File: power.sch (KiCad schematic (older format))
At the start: 3 parts

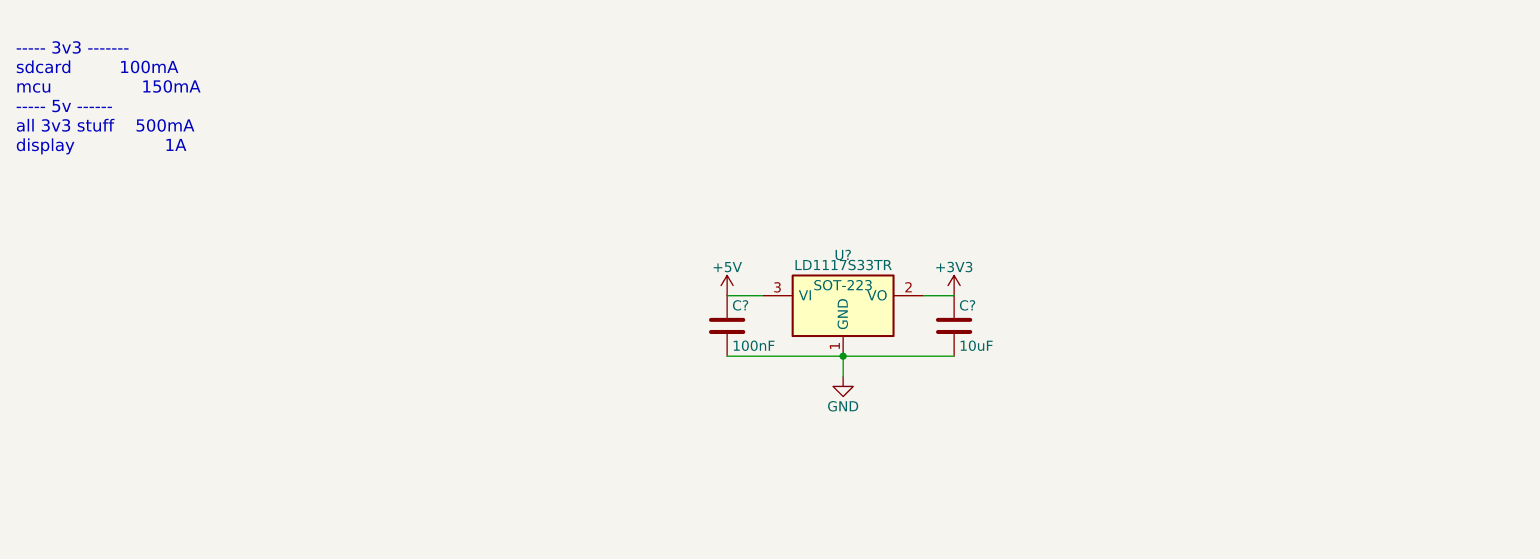
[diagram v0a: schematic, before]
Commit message: Routed a h-bridge. Damn that's a lot of work.
also assigned a lot of components.
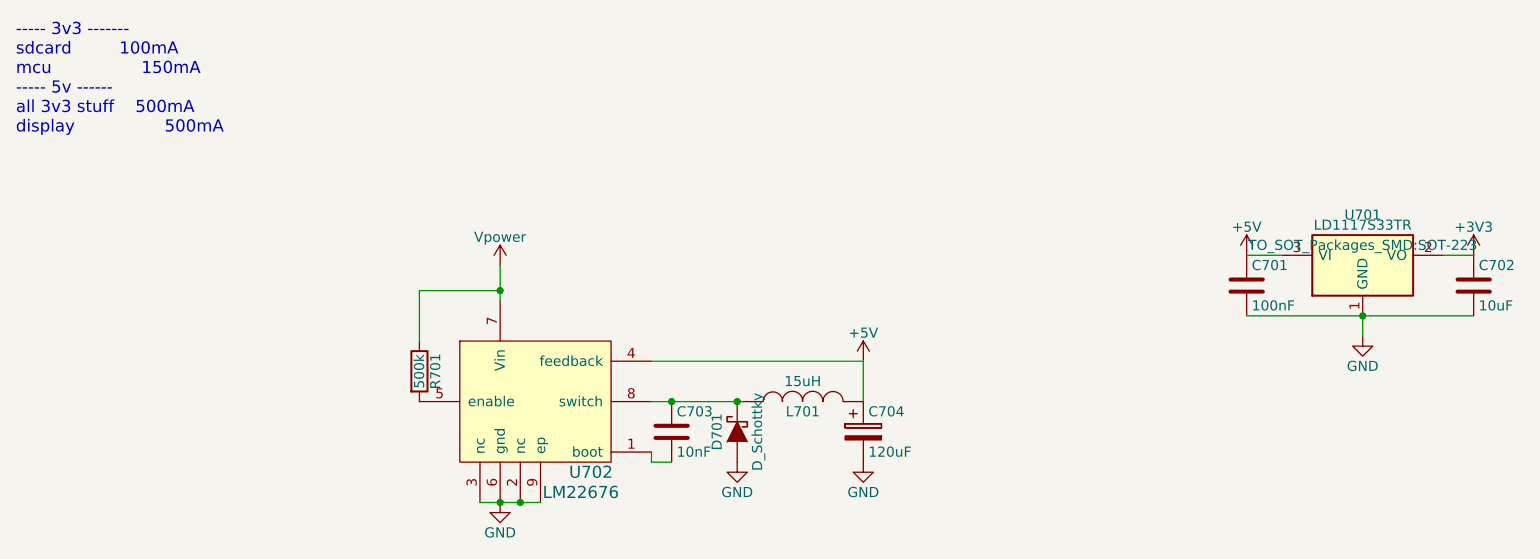
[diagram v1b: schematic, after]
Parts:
- added C703: 10nF, lib:R_0402_handsoldering, symbol C
- added C704: 120uF, Capacitors_ThroughHole:C_Radial_D5_L11_P2.5, symbol CP
- added D701: D_Schottky, Diodes_SMD:DO-214AB_Handsoldering, symbol D_Schottky
- added L701: 15uH, lib:VLS6045EX_6x6, symbol INDUCTOR
- added R701: 500k, lib:R_0402_handsoldering, symbol R
- added U702: LM22676, Housings_SOIC:SOIC-8-1EP_3.9x4.9mm_Pitch1.27mm, symbol LM22676
- C701, C702: renamed from C?; footprint (none) -> lib:R_0402_handsoldering
- U701: renamed from U?; footprint SOT-223 -> TO_SOT_Packages_SMD:SOT-223
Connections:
- net +5V: now also C704.1, L701.2, U702.4 (feedback)
- net GND: now also C704.2, D701.2 (A), U702.2 (nc), U702.3 (nc), U702.6 (gnd), U702.9 (ep)
- new net: C703.2, U702.1 (boot)
- new net: R701.2, U702.5 (enable)
- new net: C703.1, D701.1 (K), L701.1, U702.8 (switch)
- new net Vpower: R701.1, U702.7 (Vin)
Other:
- note added: "----- 3v3 -------\nsdcard 100mA\nmcu 150mA\n----- 5v ------\nall 3v3 stuff 500mA\ndisplay 500mA\n\n"
- note removed: "----- 3v3 -------\nsdcard 100mA\nmcu 150mA\n----- 5v ------\nall 3v3 stuff 500mA\ndisplay 1A\n"
- moved on the sheet: C701, C702, U701
